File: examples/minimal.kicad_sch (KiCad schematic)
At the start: 2 parts, among them U1 DemoMCU, U2 DemoSensor

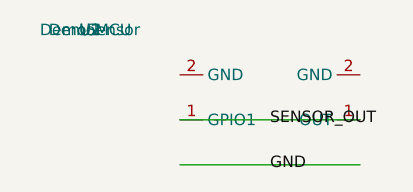
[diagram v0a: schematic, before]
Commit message: Add datasheet knowledge evidence and repeated-sheet placement fixes
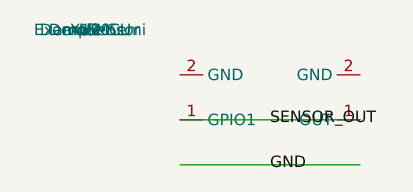
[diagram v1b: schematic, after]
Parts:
- U1: MPN (none) -> X100; Manufacturer (none) -> Example Semi
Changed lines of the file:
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@@
   (label "SENSOR_OUT" (at 20 10 0))
   (label "GND" (at 20 15 0))
-  (symbol (lib_id "MCU:DemoMCU") (at 10 10 0) (unit 1) (property "Reference" "U1") (property "Value" "DemoMCU"))
+  (symbol (lib_id "MCU:DemoMCU") (at 10 10 0) (unit 1) (property "Reference" "U1") (property "Value" "DemoMCU") (property "MPN" "X100") (property "Manufacturer" "Example Semi"))
   (symbol (lib_id "Sensor:DemoSensor") (at 30 10 0) (unit 1) (property "Reference" "U2") (property "Value" "DemoSensor")))
